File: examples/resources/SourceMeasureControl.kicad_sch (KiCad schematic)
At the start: 21 parts

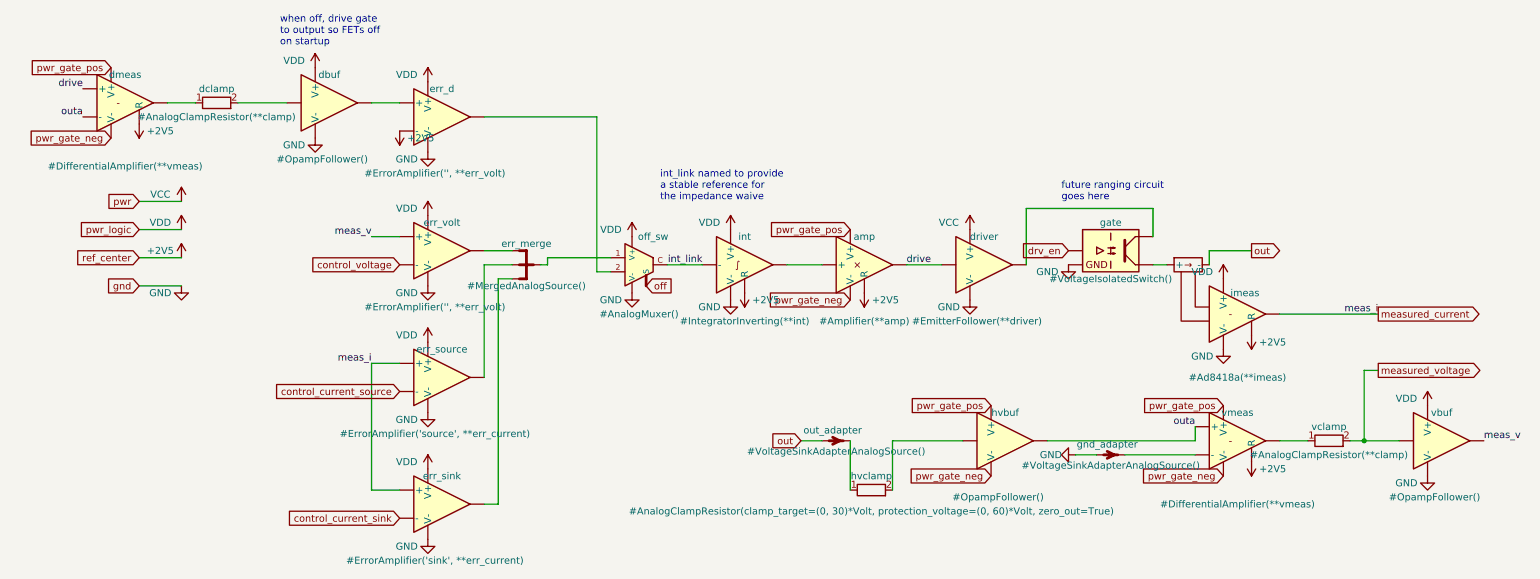
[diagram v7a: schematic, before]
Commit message: isense even if its terrible
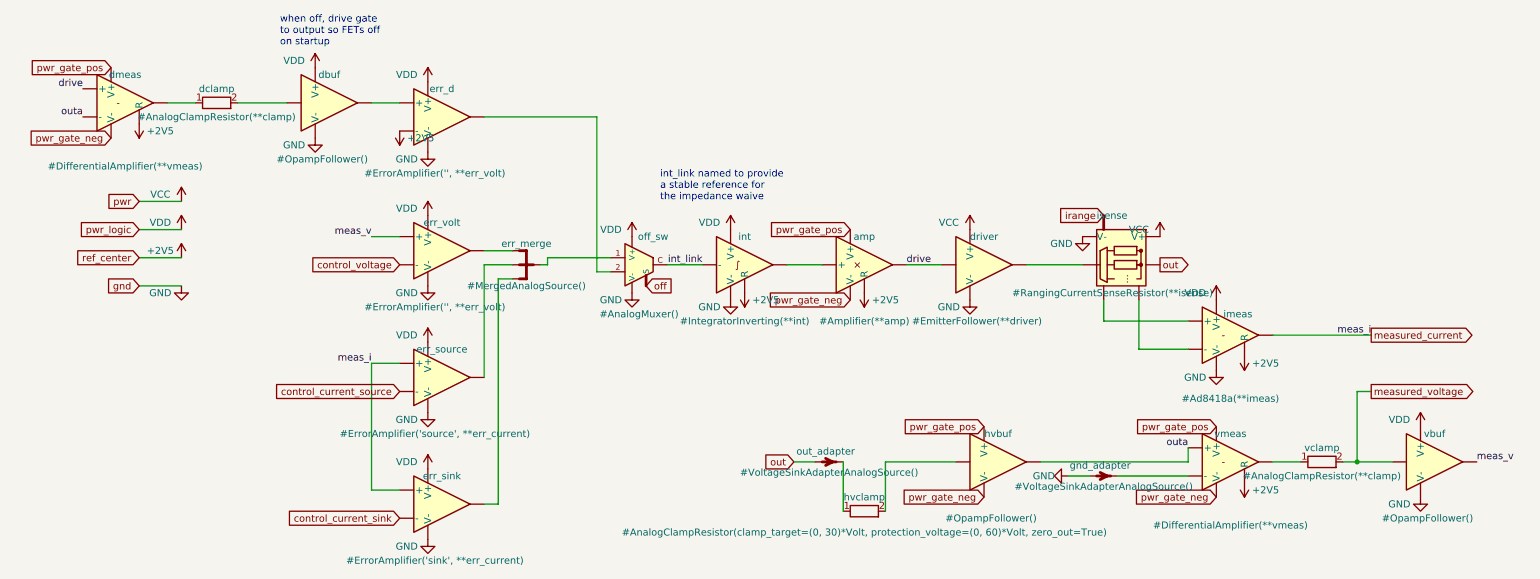
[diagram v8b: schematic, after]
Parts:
- removed gate: #VoltageIsolatedSwitch(), symbol edg_importable:VoltageIsolatedSwitch
- added isense: #RangingCurrentSenseResistor(**isense), symbol edg_importable:CurrentSenseResistorMux
- imeas: symbol edg_importable:OpampCurrentSensor -> edg_importable:DifferentialAmplifier
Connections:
- net GND: now also isense. (V-)
- net VCC: now also isense. (V-)
- net out: now also isense.com; no longer imeas.2 (-)
- net at driver.3: now also isense.sw
- net at imeas.1 (+): now also isense.sen_sw
- new net: imeas.2 (-), isense.sen_com
- new net irange: isense.control
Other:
- note removed: "future ranging circuit goes here"
- moved on the sheet: gnd_adapter, hvbuf, hvclamp, out_adapter, vbuf, vclamp, vmeas
